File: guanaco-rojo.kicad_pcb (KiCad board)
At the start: 2 copper layers, 24.4 x 40.1 mm, 21 parts, among them J1 Conn_01x02, J2 Input, J3 Output, U1 4049

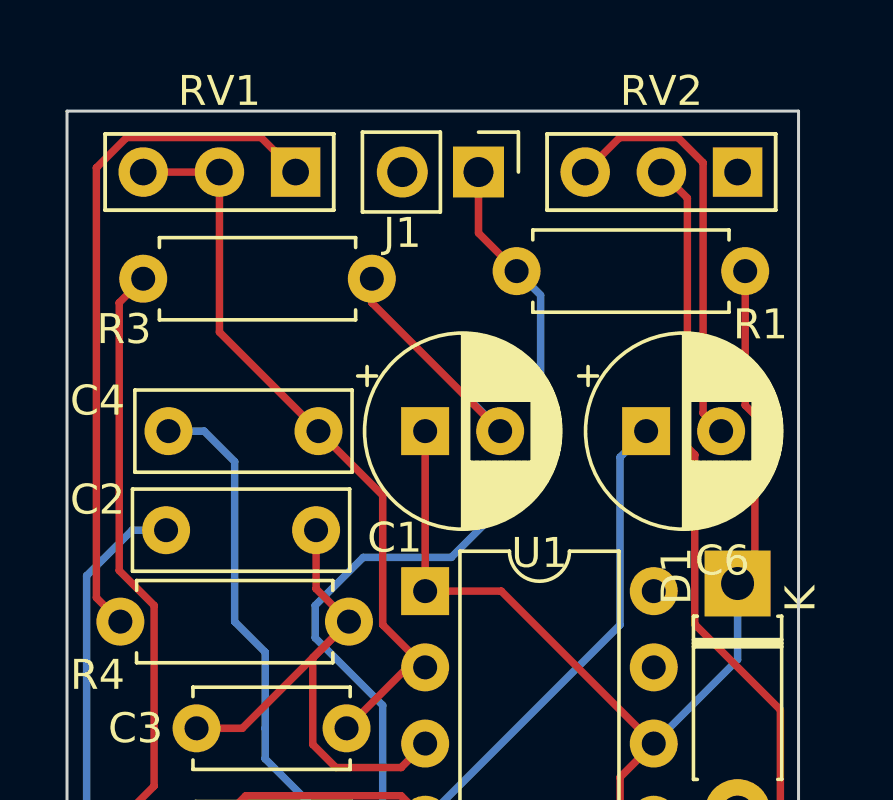
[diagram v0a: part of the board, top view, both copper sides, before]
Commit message: silkscreen markings
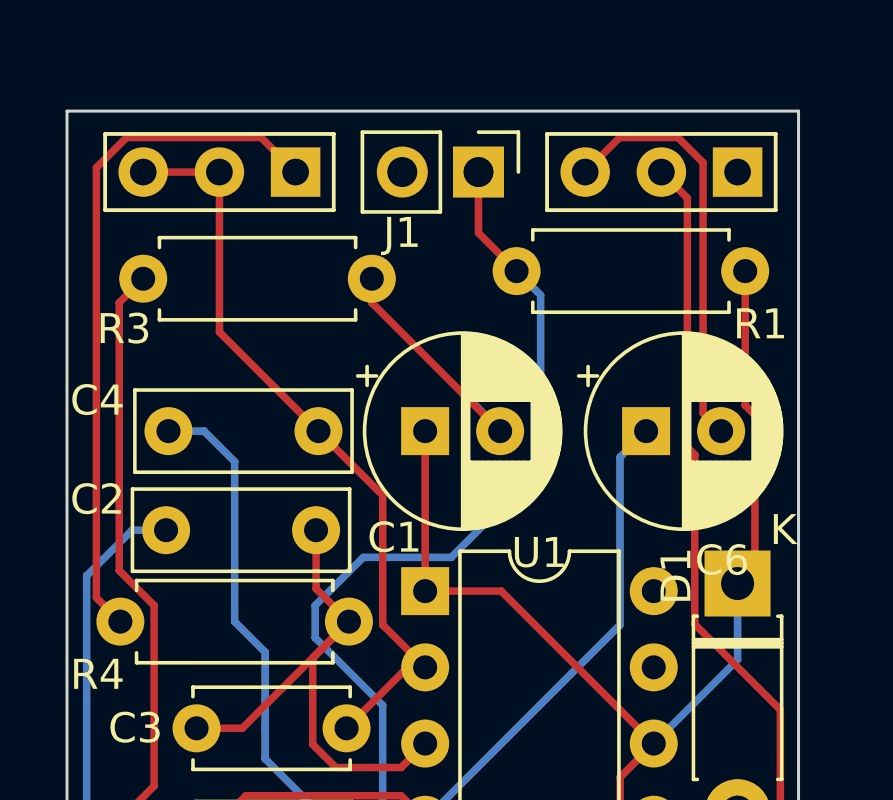
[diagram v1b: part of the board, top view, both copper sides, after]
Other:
- board text added: "1"
- board text added: "GND"
- board text added: "IN"
- board text added: "LED"
- board text added: "OUT"
- board text added: "T"
- board text added: "Vcc"
- board text added: "github.com/rockola/guanaco-rojo"
- board text removed: "github.com/rockola/GuanacoRojo"

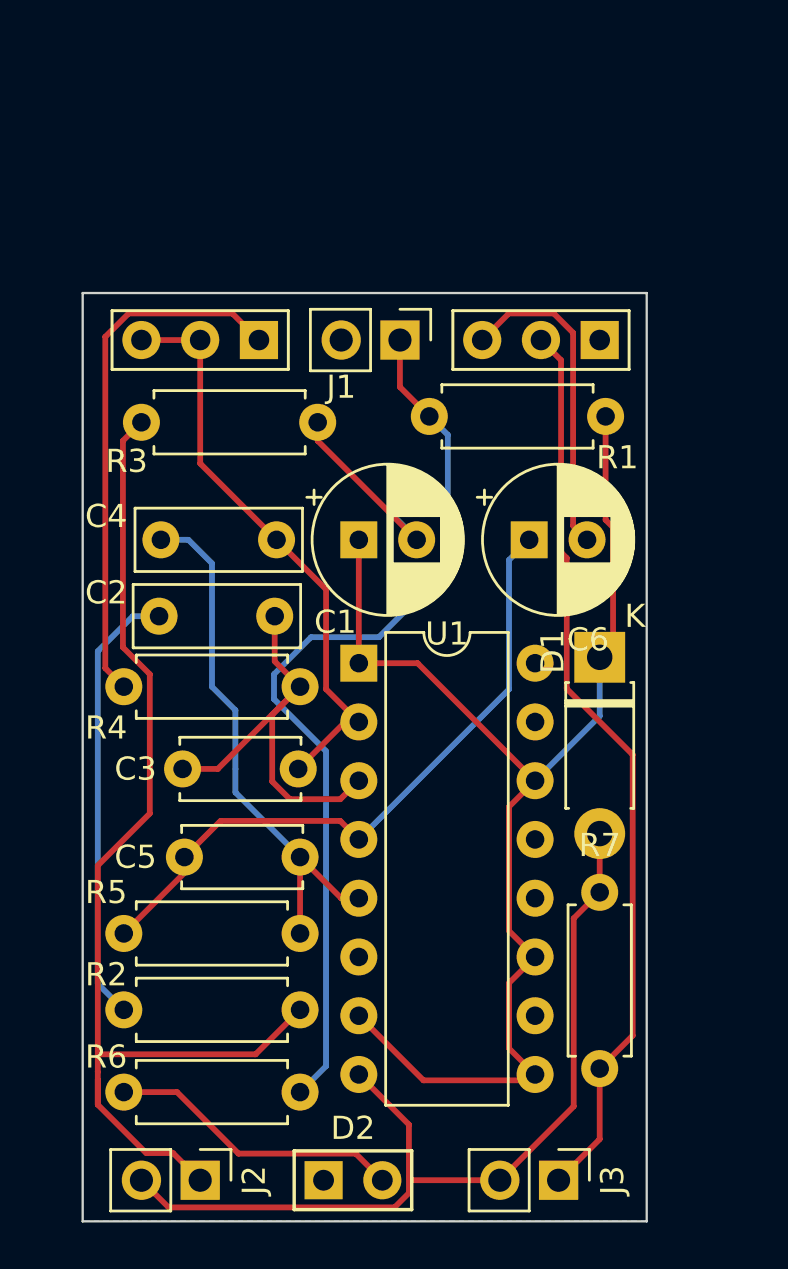
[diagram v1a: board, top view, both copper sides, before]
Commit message: v0.2: pcb rerouted for 9 mm pots, unverified
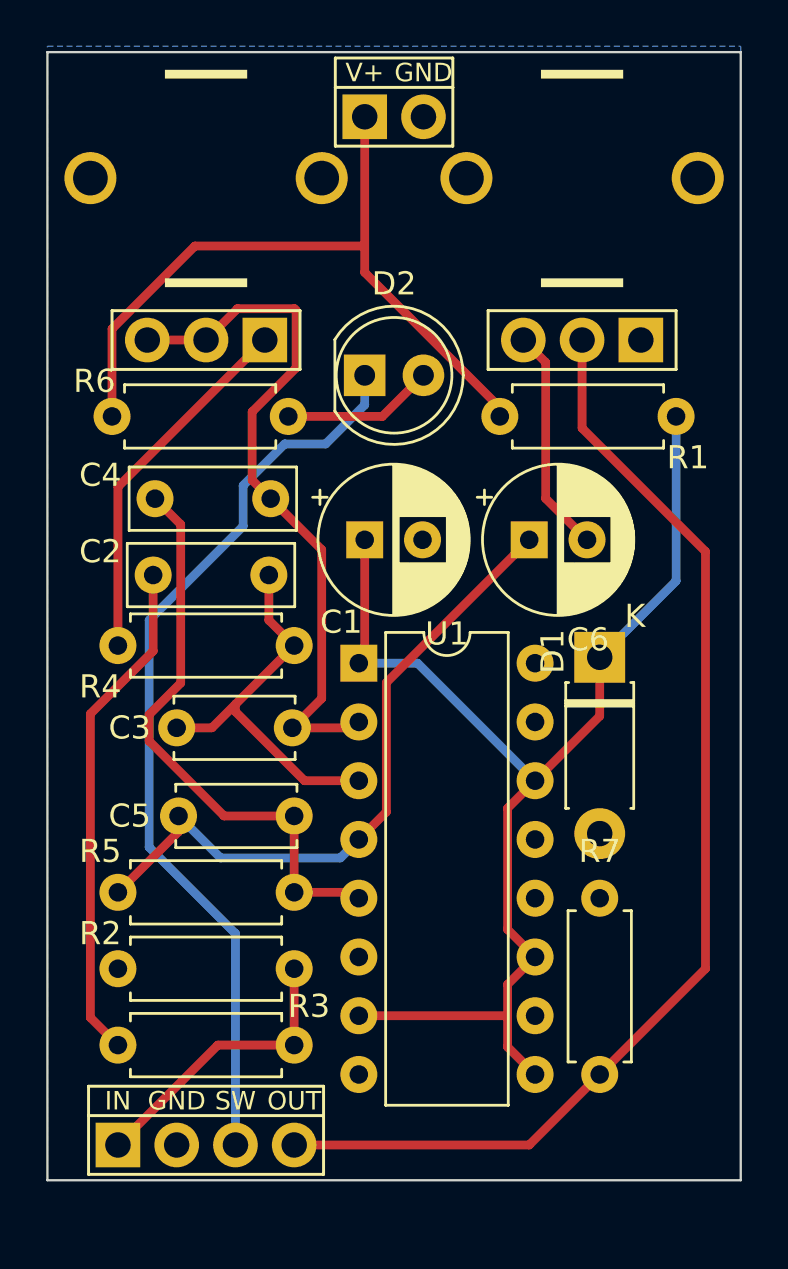
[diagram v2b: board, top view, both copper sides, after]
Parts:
- removed J3: Output, Connector_PinHeader_2.54mm:PinHeader_1x02_P2.54mm_Vertical
- D2: footprint OPL_Connector:H2-2.54 -> LED_THT:LED_D5.0mm
- J1: value Conn_01x02 -> Stomp_Connector; footprint Connector_PinHeader_2.54mm:PinHeader_1x02_P2.54mm_Vertical -> rockola_kicad_footprints:Stomp_4pin
- J2: value Input -> Power_Connector; footprint Connector_PinHeader_2.54mm:PinHeader_1x02_P2.54mm_Vertical -> rockola_kicad_footprints:Power_Header_2pin
- R2: value 100k -> 1M
- R3: value 1M -> 100k
- RV1, RV2: footprint OPL_Connector:H3-2.54 -> potentiometers:9MM_METAL_SHAFT
- moved J2 47.3 mm to (142.7, 64.3), turned to 0 degrees
- moved J1 35.8 mm to (132.1, 108.7), turned to 0 degrees
- moved D2 34.8 mm to (138.9, 75.4)
- moved R6 29.2 mm to (135.6, 77.2)
- moved R3 27.7 mm to (135.9, 104.4), turned to 180 degrees
- moved R1 3.05 mm to (144.8, 77.2)
- moved C5 1.80 mm to (135.9, 94.5)
- moved R2 1.80 mm to (135.9, 101.1)
- moved R4 1.80 mm to (135.9, 87.1)
- moved C2 1.80 mm to (129.8, 84.1)
- moved C3 1.80 mm to (130.8, 90.7)
- moved R5 1.80 mm to (135.9, 97.8)
- moved C4 1.80 mm to (134.9, 80.8)
- moved RV2 1.78 mm to (148.3, 73.9)
- moved RV1 0.25 mm to (132.1, 73.9)
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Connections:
- D2 pad 1: LED -> LED-
- J1 pad 1: +9V -> IN
- R2 pad 2: Net-(C2-Pad1) -> GND
- R3 pad 2: GND -> Net-(C2-Pad1)
- R6 pad 1: +9V -> Net-(D2-Pad2)
- R6 pad 2: Net-(D2-Pad2) -> +9V
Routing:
- net GND: track 47.4 -> 0.04 mm
- net LED-: track 0.00 -> 39.7 mm
- net IN: track 47.6 -> 12.7 mm
- net OUT: track 39.3 -> 50.3 mm
- net +9V: track 39.6 -> 31.6 mm
- net Net-(R4-Pad2): track 23.0 -> 15.8 mm
- net Net-(D2-Pad2): track 12.8 -> 6.58 mm
- net Net-(C3-Pad2): track 25.4 -> 30.6 mm
- net Net-(C6-Pad2): track 14.0 -> 9.78 mm
- net Net-(C2-Pad1): track 19.2 -> 21.9 mm
- net Net-(C2-Pad2): track 19.0 -> 16.9 mm
- net Net-(C4-Pad2): track 23.5 -> 25.3 mm
- net Net-(C1-Pad1): track 55.9 -> 54.6 mm
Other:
- board size 24.4 x 40.1 mm -> 30 x 48.8 mm
- board text added: "v0.2 2020-03-11"
- board text removed: "1"
- board text removed: "GND"
- board text removed: "IN"
- board text removed: "LED"
- board text removed: "OUT"
- board text removed: "T"
- board text removed: "Vcc"
- board text removed: "v0.1 2020-02-23"

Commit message: real v0.3 files
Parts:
- added J3: Alt. power, rockola_kicad_footprints:Power_Header_2pin, F.Cu at (126.7, 80.3)
- D2: moved to B.Cu
- J2: footprint rockola_kicad_footprints:Power_Header_2pin -> rockola_kicad_footprints:Power_Header_2pin_TOP
- U1: footprint Package_DIP:DIP-16_W7.62mm -> Package_SO:SOIC-16_3.9x9.9mm_P1.27mm
- moved J1 13.7 mm to (142.5, 99.8)
- moved D1 10.7 mm to (152.4, 77.5), turned to 180 degrees
- moved R7 10.2 mm to (148.8, 95.5)
- moved R1 10.1 mm to (152.1, 70.4), turned to 180 degrees
- moved C1 8.52 mm to (147.3, 84.1), turned to 90 degrees
- moved C3 6.90 mm to (130.0, 83.8)
- moved R6 6.86 mm to (135.9, 70.4)
- moved C6 6.04 mm to (140.2, 84.1), turned to 90 degrees
- moved U1 5.40 mm to (142.2, 91.9)
- moved C5 4.58 mm to (136.1, 89.9)
- moved R2 4.58 mm to (136.1, 96.5)
- moved R3 4.58 mm to (136.1, 99.8)
- moved R5 4.58 mm to (136.1, 93.2)
- moved C4 3.64 mm to (135.6, 77.2)
- moved C2 3.64 mm to (130.6, 80.5)
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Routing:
- net OUT: track 50.3 -> 29.7 mm
- net LED-: track 39.7 -> 24.8 mm
- net +9V: track 31.6 -> 39.5 mm
- net Net-(C5-Pad2): track 29.3 -> 22.3 mm
- net IN: track 12.7 -> 5.84 mm
- net Net-(C1-Pad1): track 54.6 -> 59.9 mm
- net Net-(C3-Pad2): track 30.6 -> 27.0 mm
- net Net-(C4-Pad2): track 25.3 -> 28.6 mm
- net Net-(C2-Pad2): track 16.9 -> 19.5 mm
- net Net-(C6-Pad2): track 9.78 -> 11.9 mm
- added copper zone on F.Cu, net GND
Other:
- board size 30 x 48.8 mm -> 30 x 40.1 mm
- board text added: "v0.3 2020-03-11"
- board text removed: "v0.2 2020-03-11"

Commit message: updated to KiCad 6.0
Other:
- net class Default removed
